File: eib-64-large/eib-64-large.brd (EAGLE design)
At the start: 40.1 x 40.4 mm, 25 parts, among them J1 DF40-REC

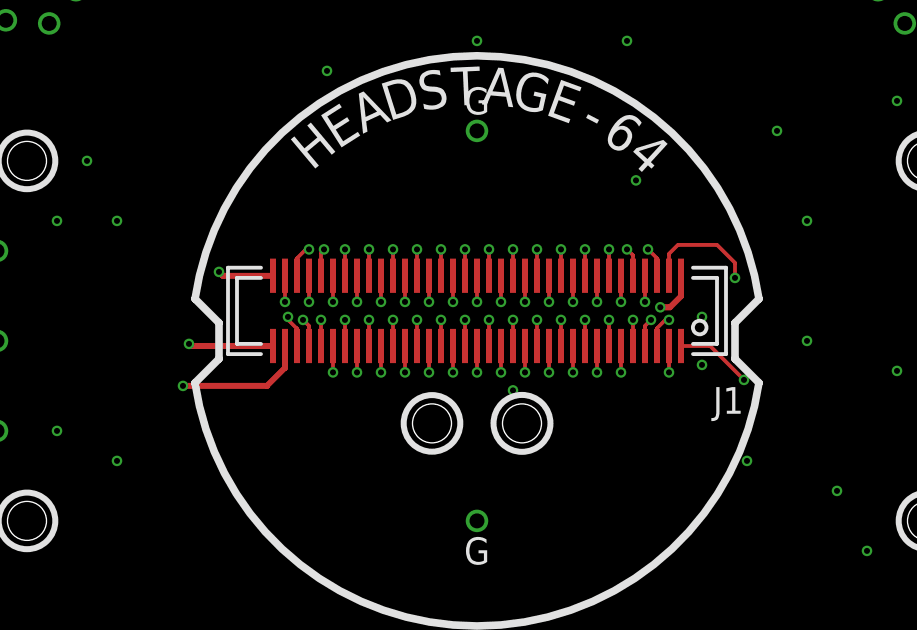
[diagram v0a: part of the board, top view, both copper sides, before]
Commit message: Update eib-64-large with Filipe's notes
- Add the version number
- Replace the connector's footprint with the expanded one used for the
omnetics-adapter-64
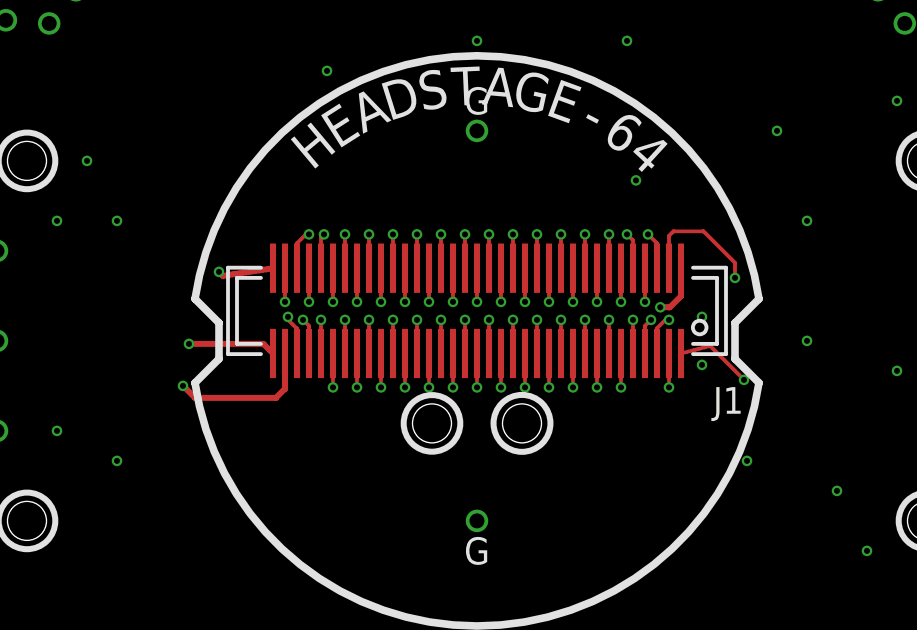
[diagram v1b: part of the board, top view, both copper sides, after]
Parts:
- J1: device jonnew:DF40-70REC -> jonnew:DDF40-70REC-LRG
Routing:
- net N$5: track 16.2 -> 15.3 mm
- net GND: track 1.52 -> 1.77 mm, vias 48 -> 47
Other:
- board text added: "EIB-64-Large"
- board text added: "Rev. 1.0 CERN OHL v1.2 JPN & Open Ephys 2019"
